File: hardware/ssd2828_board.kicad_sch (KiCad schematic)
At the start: 0 parts

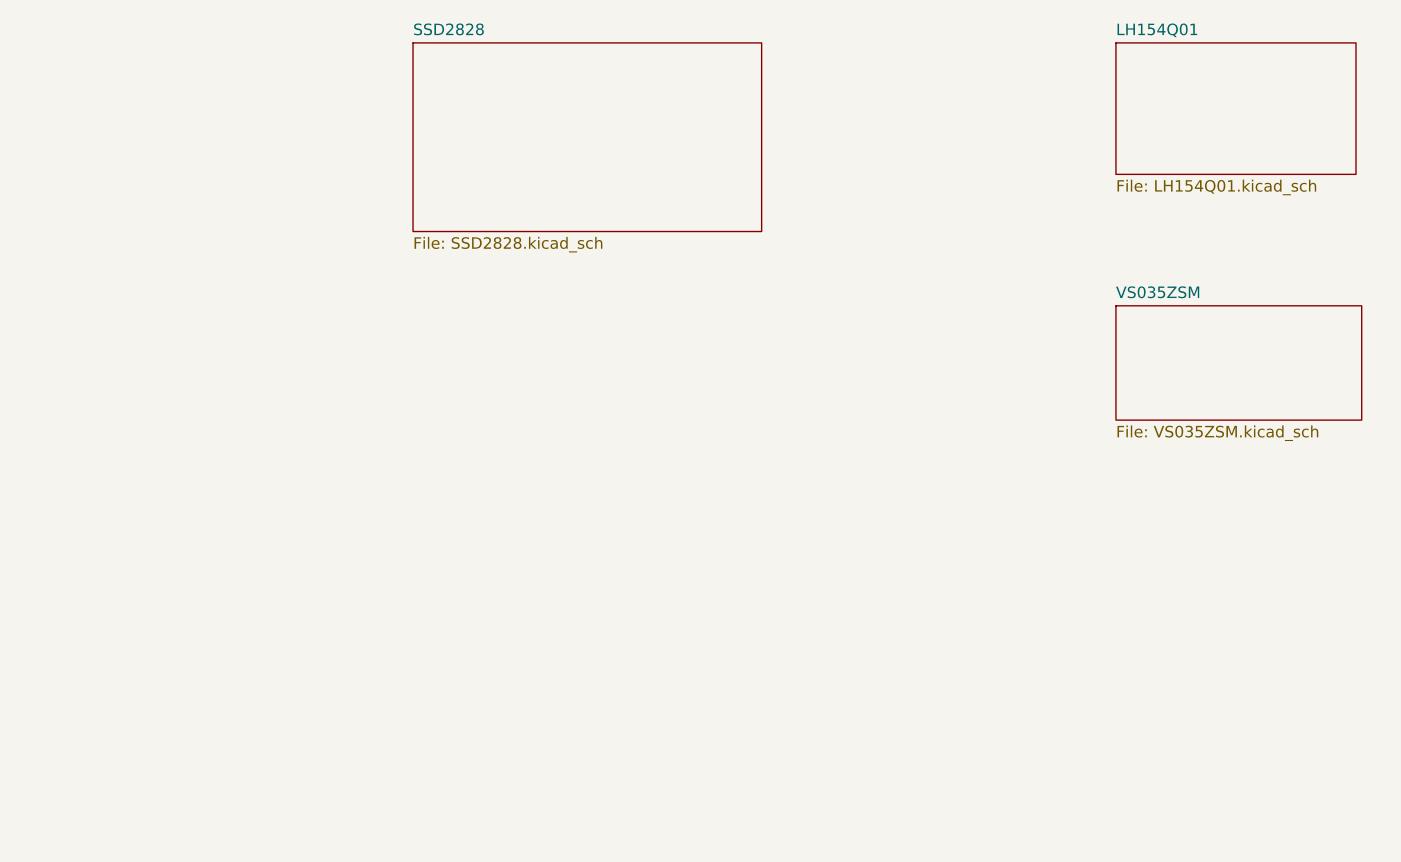
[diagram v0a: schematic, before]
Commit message: added solder bridges on all the generated voltage rails on the SSD2828 board
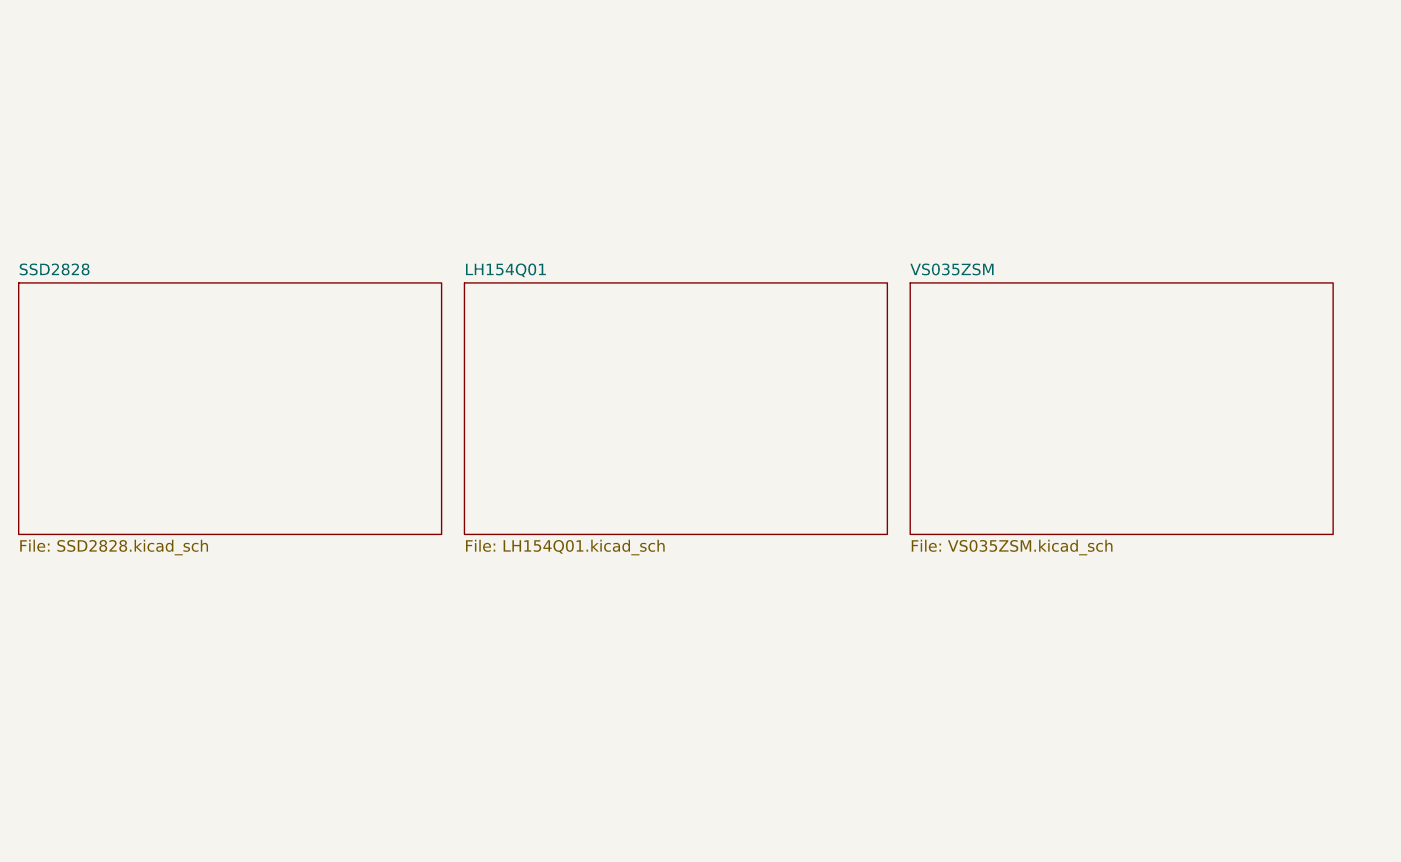
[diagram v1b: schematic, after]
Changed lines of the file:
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@@
 (kicad_sch (version 20230121) (generator eeschema)
   (paper "A4")
-  (sheet (at 198.12 83.82) (size 27.305 12.7) (fields_autoplaced)
+  (sheet (at 175.26 81.28) (size 46.99 27.94) (fields_autoplaced)
     (stroke (width 0.1524) (type solid))
     (fill (color 0 0 0 0.0000))
-    (property "Sheetname" "VS035ZSM" (at 198.12 83.1084 0)
+    (property "Sheetname" "VS035ZSM" (at 175.26 80.5684 0)
       (effects (font (size 1.27 1.27)) (justify left bottom))
     )
-    (property "Sheetfile" "VS035ZSM.kicad_sch" (at 198.12 97.1046 0)
+    (property "Sheetfile" "VS035ZSM.kicad_sch" (at 175.26 109.8046 0)
       (effects (font (size 1.27 1.27)) (justify left top))
     )
-    (property "Field2" "" (at 198.12 83.82 0)
+    (property "Field2" "" (at 175.26 81.28 0)
       (effects (font (size 1.27 1.27)) hide)
     )
@@
     )
   )
-  (sheet (at 198.12 54.61) (size 26.67 14.605) (fields_autoplaced)
+  (sheet (at 125.73 81.28) (size 46.99 27.94) (fields_autoplaced)
     (stroke (width 0.1524) (type solid))
     (fill (color 0 0 0 0.0000))
-    (property "Sheetname" "LH154Q01" (at 198.12 53.8984 0)
+    (property "Sheetname" "LH154Q01" (at 125.73 80.5684 0)
       (effects (font (size 1.27 1.27)) (justify left bottom))
     )
-    (property "Sheetfile" "LH154Q01.kicad_sch" (at 198.12 69.7996 0)
+    (property "Sheetfile" "LH154Q01.kicad_sch" (at 125.73 109.8046 0)
       (effects (font (size 1.27 1.27)) (justify left top))
     )
@@
     )
   )
-  (sheet (at 120.015 54.61) (size 38.735 20.955) (fields_autoplaced)
+  (sheet (at 76.2 81.28) (size 46.99 27.94) (fields_autoplaced)
     (stroke (width 0.1524) (type solid))
     (fill (color 0 0 0 0.0000))
-    (property "Sheetname" "SSD2828" (at 120.015 53.8984 0)
+    (property "Sheetname" "SSD2828" (at 76.2 80.5684 0)
       (effects (font (size 1.27 1.27)) (justify left bottom))
     )
-    (property "Sheetfile" "SSD2828.kicad_sch" (at 120.015 76.1496 0)
+    (property "Sheetfile" "SSD2828.kicad_sch" (at 76.2 109.8046 0)
       (effects (font (size 1.27 1.27)) (justify left top))
     )

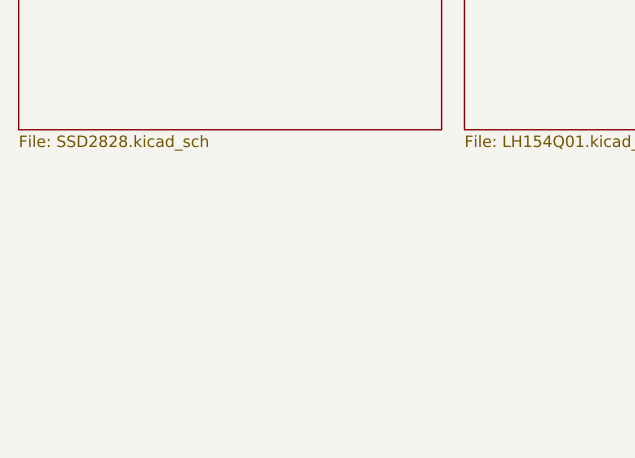
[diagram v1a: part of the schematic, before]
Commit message: fixing drc errors + adding debug board for mipi
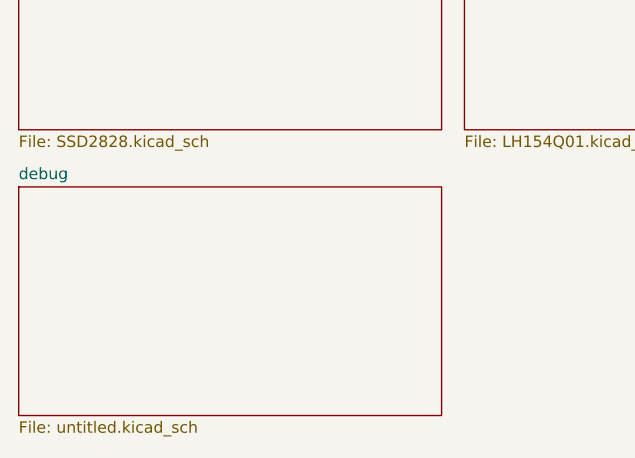
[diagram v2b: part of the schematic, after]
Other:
- added sheet debug (untitled.kicad_sch)
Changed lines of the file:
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@@
+    )
+  )
+  (sheet (at 76.2 115.57) (size 46.99 25.4) (fields_autoplaced)
+    (stroke (width 0.1524) (type solid))
+    (fill (color 0 0 0 0.0000))
+    (property "Sheetname" "debug" (at 76.2 114.8584 0)
+      (effects (font (size 1.27 1.27)) (justify left bottom))
+    )
+    (property "Sheetfile" "untitled.kicad_sch" (at 76.2 141.5546 0)
+      (effects (font (size 1.27 1.27)) (justify left top))
+    )
+    (instances
+      (project "ssd2828_board"
+        (path "/e63e39d7-6ac0-4ffd-8aa3-1841a4541b55" (page "5"))
+      )
     )
   )
